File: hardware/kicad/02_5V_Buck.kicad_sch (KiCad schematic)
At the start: 11 parts, among them U101 LMR36520ADDAR 5V/2A CANDIDATE

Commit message: Match PCB inductor to Bourns geometry and qualify current assumptions
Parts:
- L101: value 10uH Bourns SRP6030VA-100M (5A Isat) -> 10uH Bourns SRP6030VA-100M (Isat typ 5A)
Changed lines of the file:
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@@
 (symbol (lib_id "Tripmaster_Sym:L") (at 187.96 90.17 0) (unit 1) (exclude_from_sim no) (in_bom yes) (on_board yes) (dnp no)
  (property "Reference" "L101" (at 191 72.06 0) (effects (font (size 1.27 1.27))))
- (property "Value" "10uH Bourns SRP6030VA-100M (5A Isat)" (at 191 74.6 0) (effects (font (size 1.27 1.27))))
+ (property "Value" "10uH Bourns SRP6030VA-100M (Isat typ 5A)" (at 191 74.6 0) (effects (font (size 1.27 1.27))))
  (property "Footprint" "Tripmaster:L_Bourns_SRP6030VA_100M" (at 188 89.84 0) (effects (font (size 1.27 1.27)) (hide yes)))
  (pin "1") (pin "2")

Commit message: hardware(buck): replace obsolete LMR36520 sheet with actual LMR38020-Q1 400kHz 5V application circuit
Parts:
- removed C103: 1uF VCC, Tripmaster:C_1206_3216, symbol Tripmaster_Sym:C
- removed U101: LMR36520ADDAR 5V/2A CANDIDATE, Tripmaster:U3_TI_LMR36510ADDAR_DDA, symbol TripTracer_V1:LMR36520
- added R103: 64.9k 1% 400kHz, Tripmaster:R_1206_3216, symbol Tripmaster_Sym:R
- added U101: LMR38020SQDDARQ1, Package_SO:SOIC-8-1EP_3.9x4.9mm_P1.27mm_EP2.29x3mm, symbol TripTracer_V1:LMR38020_Q1
- C101: value 4.7uF 100V X7R VIN -> 4.7uF 100V X7R
- C102: value 100nF BOOT-SW -> 100nF 16V BOOT
- C104, C105: value 22uF 25V X7R VOUT -> 22uF 25V X7R
- C106: value 4.7uF 100V X7R VIN -> 22uF 25V X7R
- C107: value 220nF 100V X7R HF VIN -> 100nF 100V X7R HF
- L101: value 10uH Bourns SRP6030VA-100M (Isat typ 5A) -> 15uH / Isat>=3.8A VERIFY
- R101: value 100k 1% FB TOP TI -> 100k 1% TOP
- R102: value 24.9k 1% FB BOTTOM TI -> 24.9k 1% BOTTOM
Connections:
- net BUCK_ENABLE: now also U101.2 (EN)
- net GND: now also C101.2, C104.2, C105.2, R102.2, R103.2, U101.1 (GND), U101.9 (EP); no longer C101.1, C104.1, C105.1, R102.1
- net 5V_BUCK: now reaches R101.1
- net 5V_BUCK: now also C104.1, C105.1, C106.1, L101.2; no longer R102.2
- net BOOT_38020: now reaches C102.1
- net BOOT_38020: now also U101.7 (BOOT)
- net SW_38020: now reaches C102.2, L101.1
- net SW_38020: now also U101.8 (SW)
- removed net HV_PROTECTED_AFTER_EFUSE: C101.2, C106.1, C107.1
- removed net V5_BUCK_RAW: C104.2, C105.2, L101.2, R101.2
- new net BUCK_PG: U101.6 (PG)
- new net BUCK_VIN_PROTECTED: C101.1, C107.1, U101.3 (VIN)
- new net FB_5V: R101.2, R102.1, U101.5 (FB)
- new net RT_400KHZ: R103.1, U101.4 (RT/SYNC)
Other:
- note added: "LMR38020-Q1 5V/2A TI REV B REFERENCE: pinout GND1 EN2 VIN3 RT4 FB5 PG6 BOOT7 SW8 EP9. Provisional symbol/footprint. VIN needs external reverse and transient protection. NO VEHICLE RELEASE."
- note added: "This draft uses direct pin-end net labels. Verify ERC and native netlist before treating labels as connected. Input BAT+, ACC/HOLD, TVS and SD/USB mux NOT COMPLETE."
- note removed: "BUCK V1 TI-REFERENZ – noch KEINE Fertigungsfreigabe. EPAD, Induktor-Footprint und Bauteile pruefen."
- note removed: "HV_PROTECTED_AFTER_EFUSE ist ALTER globaler Netzname. Realer LM74930-Q1 Eingang noch NICHT verdrahtet; keine zweite eFuse."
- note removed: "NEU: BUCK_ENABLE getrennt von VIN, fuer ACC/MCU_HOLD vorgesehen. Ohne angeschlossene Enable-Steuerung kein Hochlauf; ERC/DRC offen."
- note removed: "TI Rev C Referenz: 10uH, 100k/24.9k, 2x4.7uF+220nF VIN, 2x22uF VOUT; DC-Bias/Isat/ERC noch offen."
- title: TripTracer V1 – 5 V Buck: ELEKTRISCHER ENTWURF -> TripTracer V1 - 5V Buck LMR38020-Q1

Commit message: hardware(buck): nominate low-cost 15uH 5.5A Isat inductor; explicitly flag land-pattern review
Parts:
- L101: value 15uH / Isat>=3.8A VERIFY -> 15uH FCH0650-150M Isat5.5A PROVISIONAL
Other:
- note added: "LMR38020-Q1 5V/2A TI REV B REFERENCE: pinout GND1 EN2 VIN3 RT4 FB5 PG6 BOOT7 SW8 EP9. Provisional symbol/footprint. VIN needs external reverse and transient protection. FCH0650-150M uses PROVISIONAL existing Bourns footprint: pads must be reverified. NO VEHICLE RELEASE."
- note removed: "LMR38020-Q1 5V/2A TI REV B REFERENCE: pinout GND1 EN2 VIN3 RT4 FB5 PG6 BOOT7 SW8 EP9. Provisional symbol/footprint. VIN needs external reverse and transient protection. NO VEHICLE RELEASE."

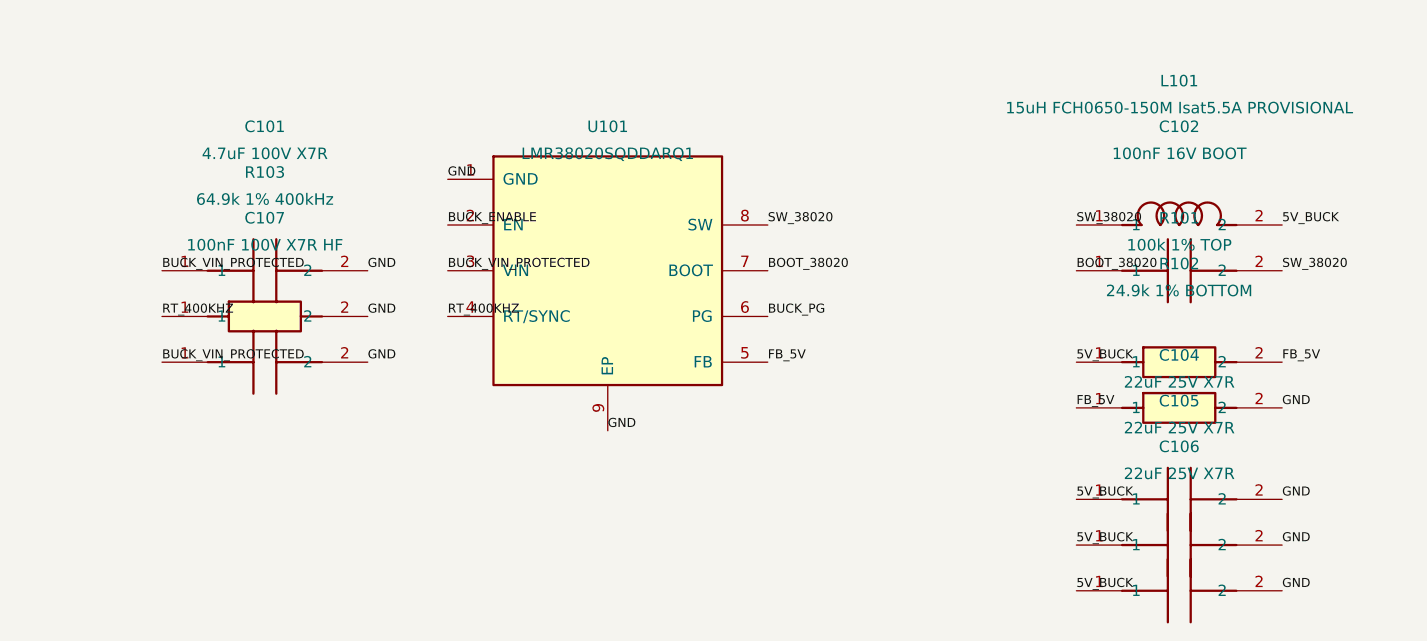
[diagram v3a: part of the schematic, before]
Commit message: hardware(buck): connect replacement LMR38020 to existing VIN, EN, GND and 5V global supply nets
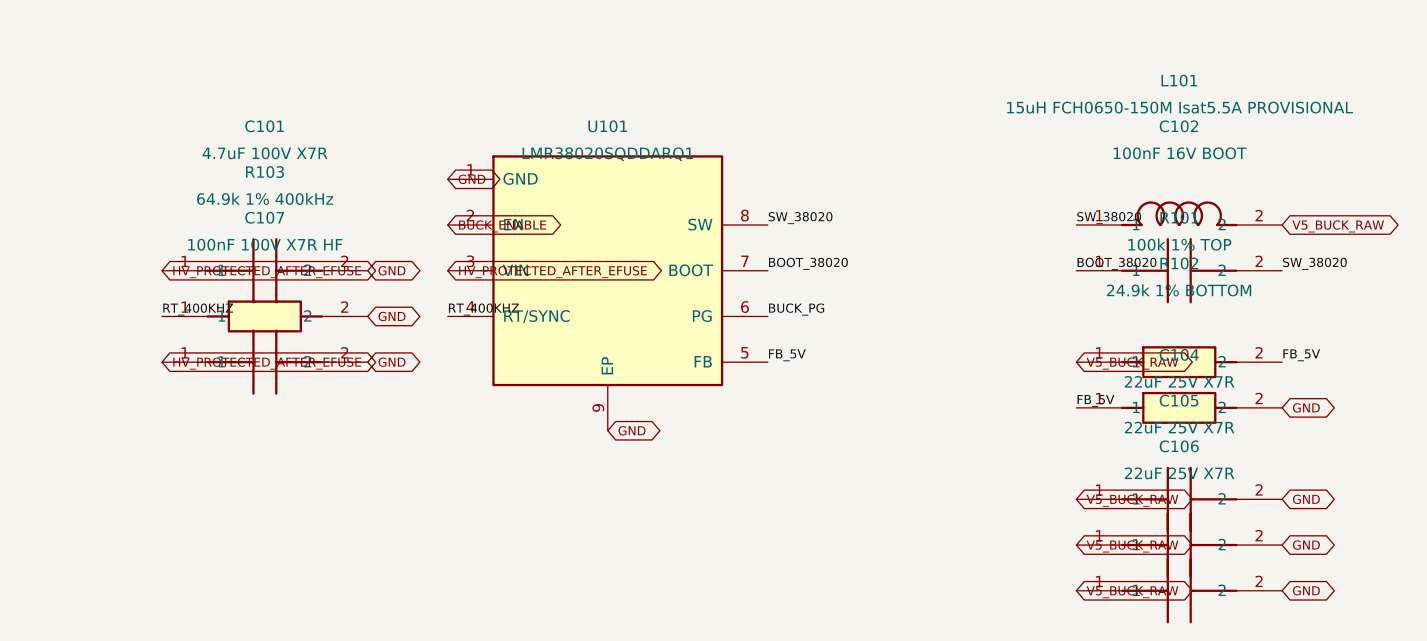
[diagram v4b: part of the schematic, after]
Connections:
- net 5V_BUCK renamed V5_BUCK_RAW
- net BUCK_VIN_PROTECTED renamed HV_PROTECTED_AFTER_EFUSE
